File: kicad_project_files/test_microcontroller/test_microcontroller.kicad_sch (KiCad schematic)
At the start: 40 parts, among them J1 USB_C_Receptacle_USB2.0, SW1 SW_Push, SW2 SW_Push, SW3 SW_Push, SW4 SW_Push, SW5 SW_Push, SW6 SW_Push, SW7 SW_Push, SW8 SW_Push, SW9 SW_Push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

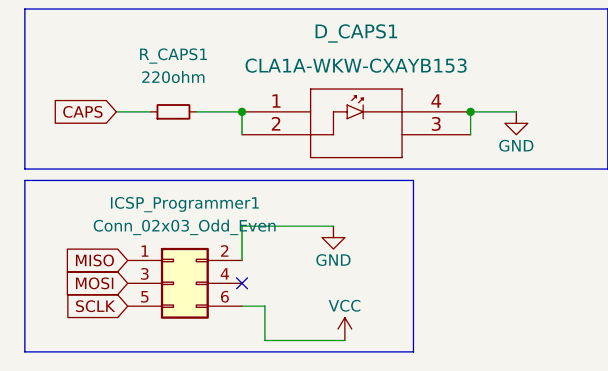
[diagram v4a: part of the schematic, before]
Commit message: update Programming pin
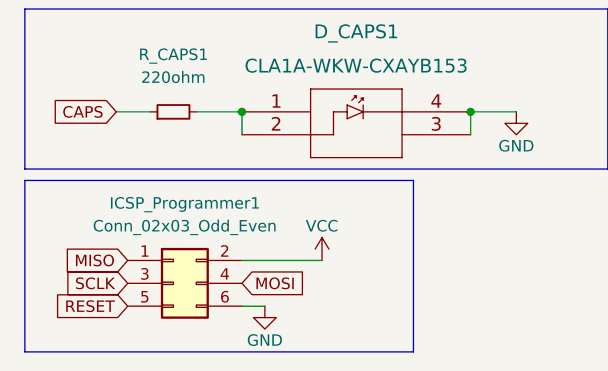
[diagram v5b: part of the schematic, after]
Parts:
- ICSP_Programmer1: footprint Connector_PinHeader_2.00mm:PinHeader_2x03_P2.00mm_Vertical -> Connector_PinHeader_2.54mm:PinHeader_2x03_P2.54mm_Vertical
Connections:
- net GND: now also ICSP_Programmer1.6 (Pin_6); no longer ICSP_Programmer1.2 (Pin_2)
- net MOSI: now also ICSP_Programmer1.4 (Pin_4); no longer ICSP_Programmer1.3 (Pin_3)
- net RESET: now also ICSP_Programmer1.5 (Pin_5)
- net SCLK: now also ICSP_Programmer1.3 (Pin_3); no longer ICSP_Programmer1.5 (Pin_5)
- net VCC: now also ICSP_Programmer1.2 (Pin_2); no longer ICSP_Programmer1.6 (Pin_6)
- no-connect marks 13 -> 12
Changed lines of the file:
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@@
   (no_connect (at 250.19 90.17))
   (no_connect (at 250.19 107.95))
-  (no_connect (at 38.1 180.34))
   (no_connect (at 250.19 87.63))
   (no_connect (at 250.19 110.49))
@@
   (no_connect (at 250.19 105.41))
   (no_connect (at 250.19 85.09))
-  (wire (pts (xy 40.64 182.88) (xy 40.64 186.69))
-    (stroke (width 0) (type default) (color 0 0 0 0))
-  )
   (wire (pts (xy 24.13 19.05) (xy 24.13 21.59))
     (stroke (width 0) (type default) (color 0 0 0 0))
@@
     (stroke (width 0) (type default) (color 0 0 0 0))
   )
-  (wire (pts (xy 49.53 186.69) (xy 40.64 186.69))
-    (stroke (width 0) (type default) (color 0 0 0 0))
-  )
   (wire (pts (xy 36.83 29.21) (xy 40.64 29.21))
     (stroke (width 0) (type default) (color 0 0 0 0))
@@
     (stroke (width 0) (type default) (color 0 0 0 0))
   )
-  (wire (pts (xy 38.1 173.99) (xy 38.1 177.8))
-    (stroke (width 0) (type default) (color 0 0 0 0))
-  )
   (wire (pts (xy 22.86 140.97) (xy 27.94 140.97))
     (stroke (width 0) (type default) (color 0 0 0 0))
@@
     (stroke (width 0) (type default) (color 0 0 0 0))
   )
+  (wire (pts (xy 38.1 177.8) (xy 46.99 177.8))
+    (stroke (width 0) (type default) (color 0 0 0 0))
+  )
   (wire (pts (xy 38.1 182.88) (xy 40.64 182.88))
     (stroke (width 0) (type default) (color 0 0 0 0))
@@
   )
   (polyline (pts (xy 45.72 35.56) (xy 45.72 12.7))
-    (stroke (width 0) (type default) (color 0 0 0 0))
-  )
-  (wire (pts (xy 48.26 173.99) (xy 38.1 173.99))
     (stroke (width 0) (type default) (color 0 0 0 0))
   )
@@
     )
   )
+  (global_label "RESET" (shape input) (at 25.4 182.88 180) (fields_autoplaced)
+    (effects (font (size 1.27 1.27)) (justify right))
+    (property "Intersheet References" "${INTERSHEET_REFS}" (id 0) (at 17.2417 182.8006 0)
+      (effects (font (size 1.27 1.27)) (justify right) hide)
+    )
+  )
   (global_label "D-" (shape input) (at 158.75 63.5 0) (fields_autoplaced)
     (effects (font (size 1.27 1.27)) (justify left))
@@
     )
   )
+  (global_label "MOSI" (shape input) (at 38.1 180.34 0) (fields_autoplaced)
+    (effects (font (size 1.27 1.27)) (justify left))
+    (property "Intersheet References" "${INTERSHEET_REFS}" (id 0) (at 45.1093 180.2606 0)
+      (effects (font (size 1.27 1.27)) (justify left) hide)
+    )
+  )
   (global_label "ROW2" (shape input) (at 250.19 115.57 0) (fields_autoplaced)
     (effects (font (size 1.27 1.27)) (justify left))
@@
     )
   )
+  (global_label "SCLK" (shape input) (at 25.4 180.34 180) (fields_autoplaced)
+    (effects (font (size 1.27 1.27)) (justify right))
+    (property "Intersheet References" "${INTERSHEET_REFS}" (id 0) (at 18.2093 180.4194 0)
+      (effects (font (size 1.27 1.27)) (justify right) hide)
+    )
+  )
   (global_label "RESET" (shape input) (at 214.63 82.55 180) (fields_autoplaced)
     (effects (font (size 1.27 1.27)) (justify right))
@@
     )
   )
-  (global_label "MOSI" (shape input) (at 25.4 180.34 180) (fields_autoplaced)
-    (effects (font (size 1.27 1.27)) (justify right))
-    (property "Intersheet References" "${INTERSHEET_REFS}" (id 0) (at 18.3907 180.4194 0)
-      (effects (font (size 1.27 1.27)) (justify right) hide)
-    )
-  )
-  (global_label "SCLK" (shape input) (at 25.4 182.88 180) (fields_autoplaced)
-    (effects (font (size 1.27 1.27)) (justify right))
-    (property "Intersheet References" "${INTERSHEET_REFS}" (id 0) (at 18.2093 182.9594 0)
-      (effects (font (size 1.27 1.27)) (justify right) hide)
-    )
-  )
   (global_label "COL3" (shape input) (at 250.19 97.79 0) (fields_autoplaced)
     (effects (font (size 1.27 1.27)) (justify left))
@@
     (pin "2")
   )
-  (symbol (lib_id "power:GND") (at 48.26 173.99 0) (unit 1)
-    (in_bom yes) (on_board yes) (fields_autoplaced)
-    (property "Reference" "#PWR09" (id 0) (at 48.26 180.34 0)
-      (effects (font (size 1.27 1.27)) hide)
-    )
-    (property "Value" "GND" (id 1) (at 48.26 177.8 0))
-    (property "Footprint" "" (id 2) (at 48.26 173.99 0)
-      (effects (font (size 1.27 1.27)) hide)
-    )
-    (property "Datasheet" "" (id 3) (at 48.26 173.99 0)
-      (effects (font (size 1.27 1.27)) hide)
-    )
-    (pin "1")
-  )
   (symbol (lib_id "Device:C") (at 25.4 50.8 0) (unit 1)
     (in_bom yes) (on_board yes) (fields_autoplaced)
@@
     (property "Reference" "ICSP_Programmer1" (id 0) (at 31.75 171.45 0))
     (property "Value" "Conn_02x03_Odd_Even" (id 1) (at 31.75 173.99 0))
-    (property "Footprint" "Connector_PinHeader_2.00mm:PinHeader_2x03_P2.00mm_Vertical" (id 2) (at 30.48 180.34 0)
+    (property "Footprint" "Connector_PinHeader_2.54mm:PinHeader_2x03_P2.54mm_Vertical" (id 2) (at 30.48 180.34 0)
       (effects (font (size 1.27 1.27)) hide)
     )
@@
     (pin "2")
   )
+  (symbol (lib_id "power:GND") (at 40.64 182.88 0) (unit 1)
+    (in_bom yes) (on_board yes) (fields_autoplaced)
+    (property "Reference" "#PWR?" (id 0) (at 40.64 189.23 0)
+      (effects (font (size 1.27 1.27)) hide)
+    )
+    (property "Value" "GND" (id 1) (at 40.64 186.69 0))
+    (property "Footprint" "" (id 2) (at 40.64 182.88 0)
+      (effects (font (size 1.27 1.27)) hide)
+    )
+    (property "Datasheet" "" (id 3) (at 40.64 182.88 0)
+      (effects (font (size 1.27 1.27)) hide)
+    )
+    (pin "1")
+  )
   (symbol (lib_id "Switch:SW_Push") (at 52.07 130.81 0) (unit 1)
     (in_bom yes) (on_board yes) (fields_autoplaced)
@@
     )
     (property "Datasheet" "" (id 3) (at 187.96 97.79 0)
+      (effects (font (size 1.27 1.27)) hide)
+    )
+    (pin "1")
+  )
+  (symbol (lib_id "power:VCC") (at 46.99 177.8 0) (unit 1)
+    (in_bom yes) (on_board yes) (fields_autoplaced)
+    (property "Reference" "#PWR?" (id 0) (at 46.99 181.61 0)
+      (effects (font (size 1.27 1.27)) hide)
+    )
+    (property "Value" "VCC" (id 1) (at 46.99 173.99 0))
+    (property "Footprint" "" (id 2) (at 46.99 177.8 0)
+      (effects (font (size 1.27 1.27)) hide)
+    )
+    (property "Datasheet" "" (id 3) (at 46.99 177.8 0)
       (effects (font (size 1.27 1.27)) hide)
     )
@@
     (pin "2")
   )
-  (symbol (lib_id "power:VCC") (at 49.53 186.69 0) (unit 1)
-    (in_bom yes) (on_board yes) (fields_autoplaced)
-    (property "Reference" "#PWR010" (id 0) (at 49.53 190.5 0)
-      (effects (font (size 1.27 1.27)) hide)
-    )
-    (property "Value" "VCC" (id 1) (at 49.53 182.88 0))
-    (property "Footprint" "" (id 2) (at 49.53 186.69 0)
-      (effects (font (size 1.27 1.27)) hide)
-    )
-    (property "Datasheet" "" (id 3) (at 49.53 186.69 0)
-      (effects (font (size 1.27 1.27)) hide)
-    )
-    (pin "1")
-  )
   (symbol (lib_id "power:GND") (at 208.28 114.3 0) (unit 1)
     (in_bom yes) (on_board yes) (fields_autoplaced)
@@
       (reference "#PWR08") (unit 1) (value "GND") (footprint "")
     )
-    (path "/0db4c658-cce5-4054-86a1-1dda33675c26"
-      (reference "#PWR09") (unit 1) (value "GND") (footprint "")
-    )
-    (path "/d26e8902-207a-45d3-9cc8-035ef9ae29e9"
-      (reference "#PWR010") (unit 1) (value "VCC") (footprint "")
-    )
     (path "/a717bee7-1902-40ae-b673-fad1ccbf129c"
       (reference "#PWR0101") (unit 1) (value "GND") (footprint "")
@@
       (reference "#PWR0107") (unit 1) (value "GND") (footprint "")
     )
+    (path "/48377bbf-9e70-4cc4-9883-0d15cd8542d9"
+      (reference "#PWR?") (unit 1) (value "GND") (footprint "")
+    )
+    (path "/59e922ed-b3fc-472a-8e22-6ef5736fb51f"
+      (reference "#PWR?") (unit 1) (value "VCC") (footprint "")
+    )
     (path "/4d48e41d-3878-4a27-ab4f-51a7ebfea6fe"
       (reference "C1") (unit 1) (value "0.1uf") (footprint "Capacitor_THT:C_Rect_L7.0mm_W2.0mm_P5.00mm")
@@
     )
     (path "/1bc5dd36-6c22-4532-936b-9ec262629ce9"
-      (reference "ICSP_Programmer1") (unit 1) (value "Conn_02x03_Odd_Even") (footprint "Connector_PinHeader_2.00mm:PinHeader_2x03_P2.00mm_Vertical")
+      (reference "ICSP_Programmer1") (unit 1) (value "Conn_02x03_Odd_Even") (footprint "Connector_PinHeader_2.54mm:PinHeader_2x03_P2.54mm_Vertical")
     )
     (path "/29e44f23-b958-4c15-8e4c-23c54ef10f8f"

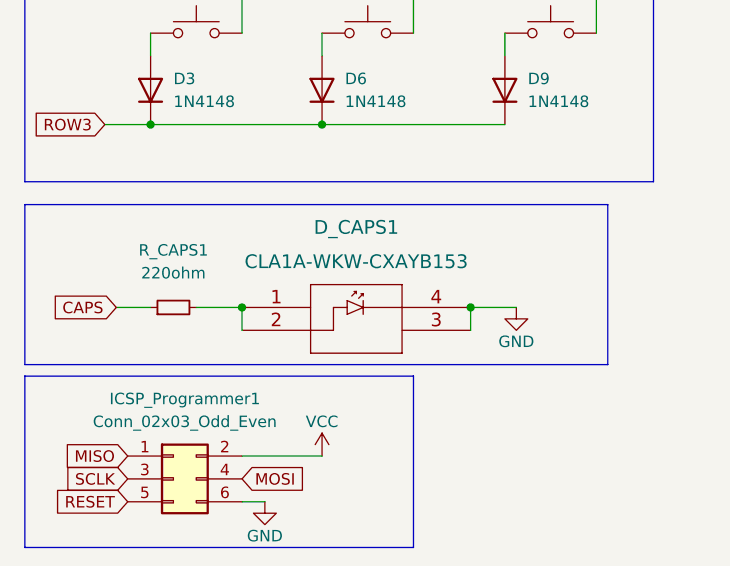
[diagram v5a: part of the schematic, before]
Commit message: redesign icsp
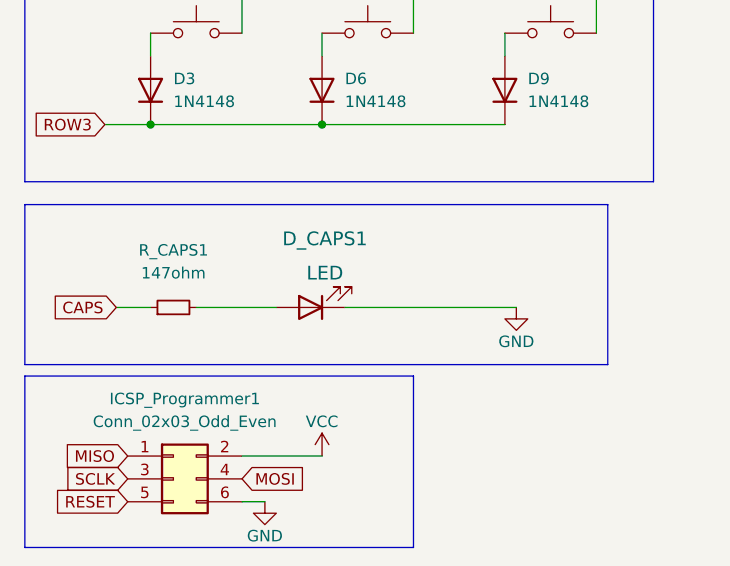
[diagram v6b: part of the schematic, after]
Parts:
- D_CAPS1: value CLA1A-WKW-CXAYB153 -> LED; footprint LED_SMD:LED_Cree-PLCC4_3.2x2.8mm_CCW -> LED_THT:LED_D3.0mm; symbol CLA1A-WKW-CXAYB153 (SMD_LED):CLA1A-WKW-CXAYB153 -> Device:LED
- R1, R2, R3, R4, R5, R6, R7: footprint Resistor_THT:R_Axial_DIN0204_L3.6mm_D1.6mm_P5.08mm_Horizontal -> Resistor_THT:R_Axial_DIN0204_L3.6mm_D1.6mm_P7.62mm_Horizontal
- R_CAPS1: value 220ohm -> 147ohm; footprint Resistor_THT:R_Axial_DIN0204_L3.6mm_D1.6mm_P5.08mm_Horizontal -> Resistor_THT:R_Axial_DIN0204_L3.6mm_D1.6mm_P7.62mm_Horizontal
- SW1: footprint Button_Switch_THT:SW_PUSH_6mm -> Button - Alternate:SW_4-1437565-0
- Y1: footprint Crystal:Crystal_SMD_HC49-SD -> Crystal:Crystal_SMD_HC49-SD_HandSoldering
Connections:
- net GND: now also D_CAPS1.1 (K); no longer D_CAPS1.3, D_CAPS1.4
- net at D_CAPS1.2 (A), R_CAPS1.2: no longer D_CAPS1.1
